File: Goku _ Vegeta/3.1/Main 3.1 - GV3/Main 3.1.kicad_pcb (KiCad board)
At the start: 2 copper layers, 206 x 197.4 mm, 64 parts, among them J1 Battery Buzzer, J10 Motor 4, J11 LEFT HEADERS, J12 RIGHT HEADERS, J13 MID HEADERS, J14 UART, J15 I2C, J16 4S Battery, J17 Power Switch, J18 Batt Bal, J19 5V PI, J2 5V LINE, J20 ESC PWR, J23 ESC PWM, J3 BACKUP 3V3, J4 I2C, J5 SPI, J6 Solenoid, J7 Motor 1, J8 Motor 2, J9 Motor 3, Q1 BSC040N10NS5, Q2 Q_Photo_NPN, U13 Adafruit_BNO055_STEMMA_QT, U4 TB67H420FTG Dual/Single Motor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, U5 TB67H420FTG Dual/Single Motor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, U6 TB67H420FTG Dual/Single Motor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, U7 TB67H420FTG Dual/Single Motor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, U8 DEV-16771, U9 Arduino Compatible DC-DC Boos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

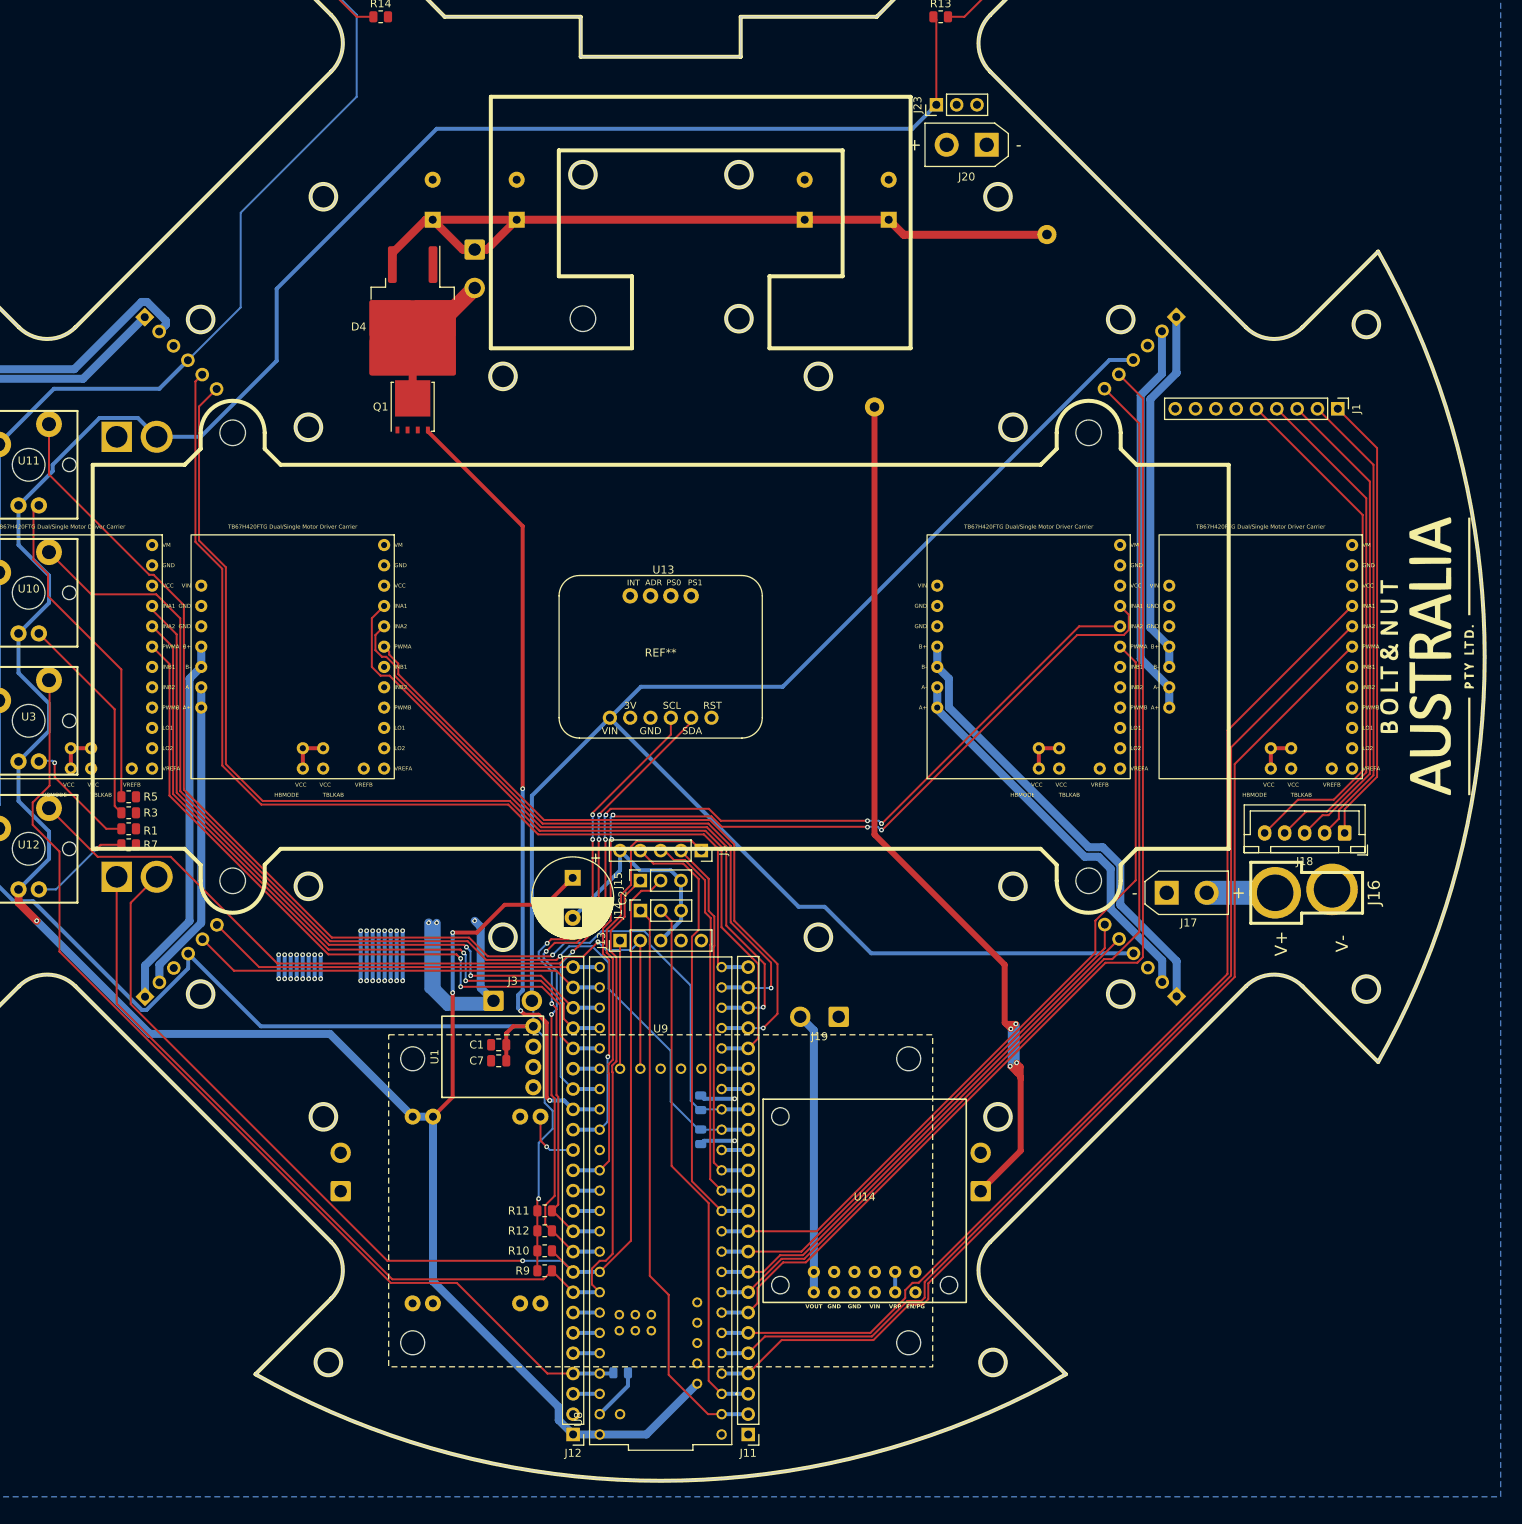
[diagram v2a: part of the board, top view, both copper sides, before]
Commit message: Main and Line 3.1 done w/ silkscreen
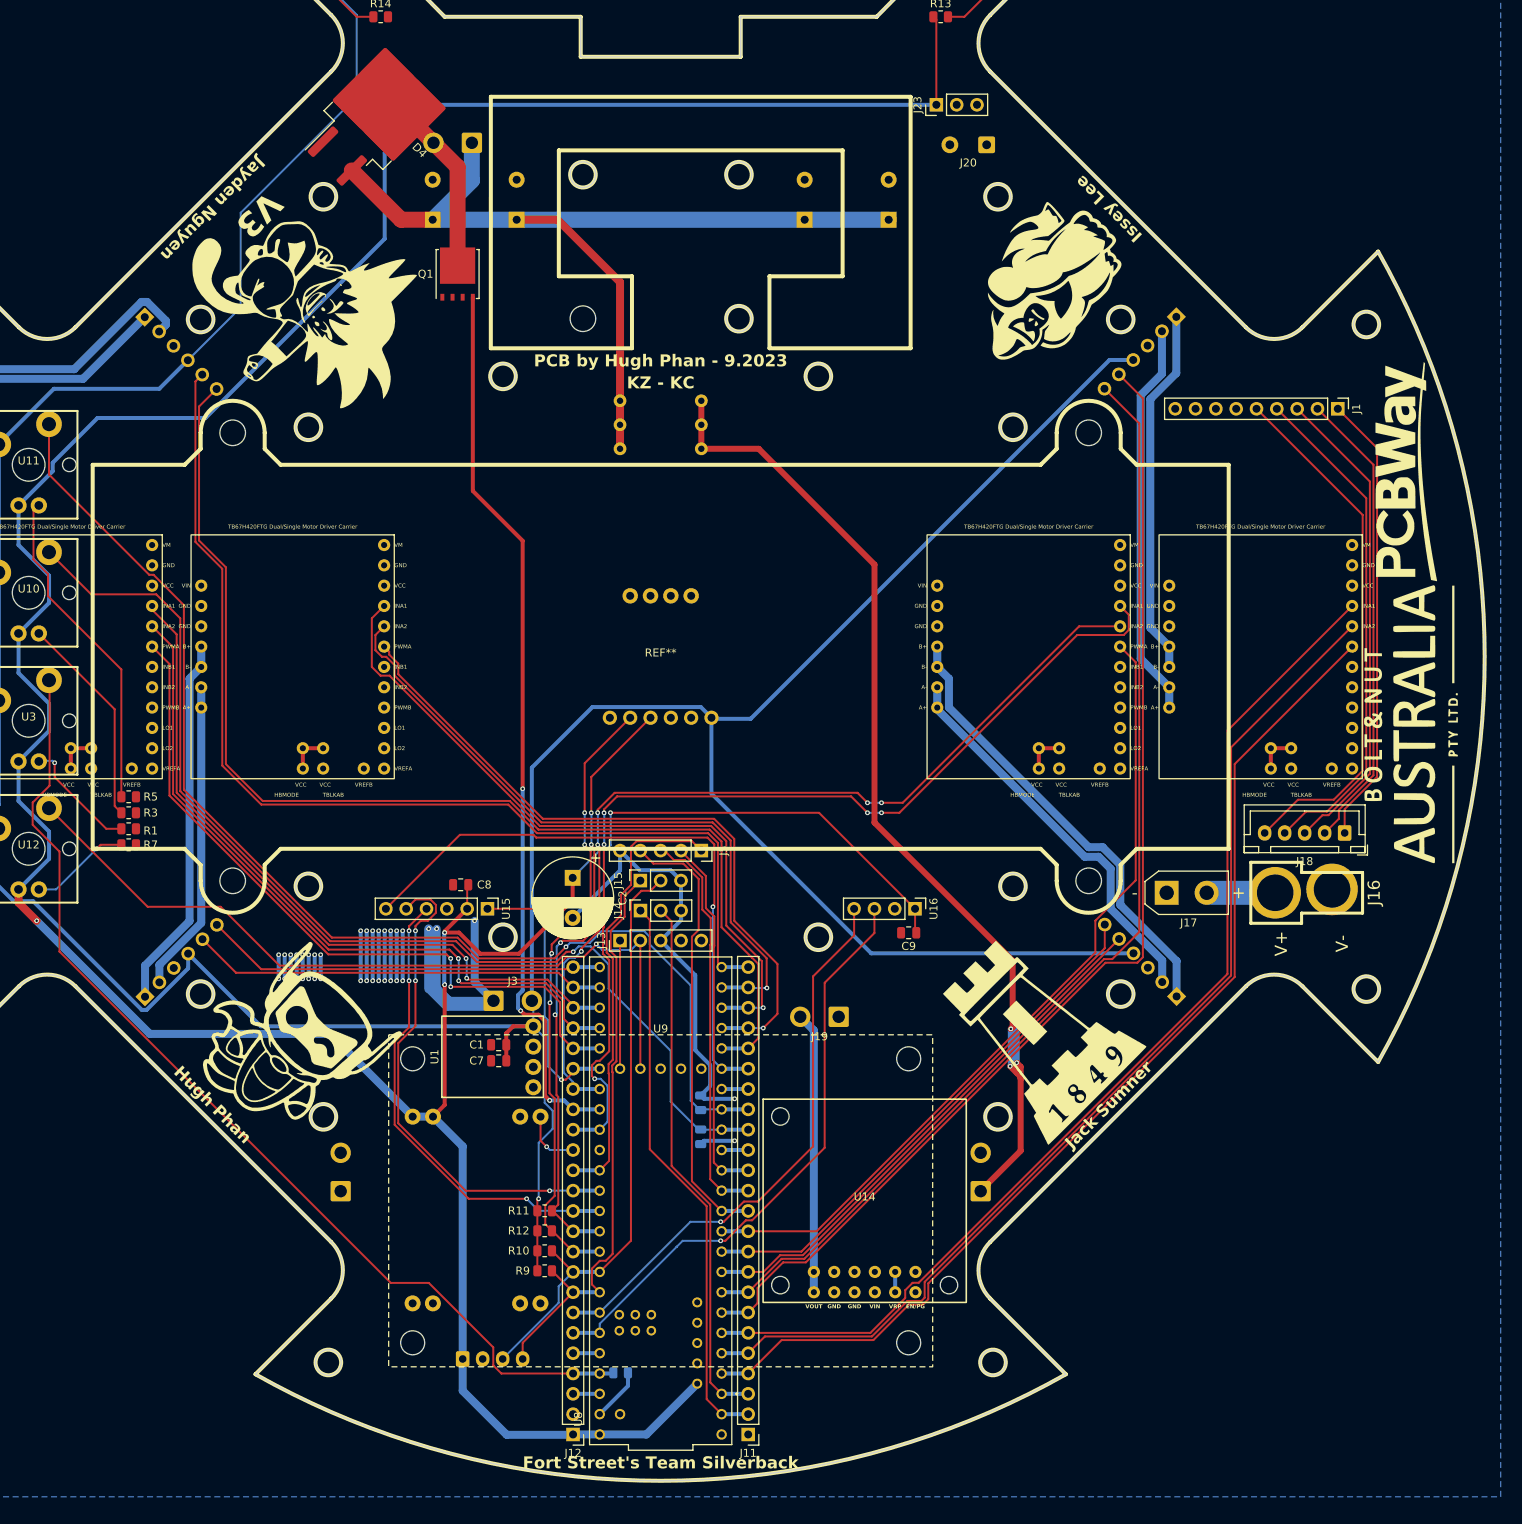
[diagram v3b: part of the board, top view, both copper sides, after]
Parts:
- removed the G*** at (245.5, 150.0)
- removed J2: 5V LINE, Connector_AMASS:AMASS_XT30U-F_1x02_P5.0mm_Vertical
- removed J4: I2C, Connector_AMASS:AMASS_XT30U-F_1x02_P5.0mm_Vertical
- added C8: 10uF, Capacitor_SMD:C_0805_2012Metric, F.Cu at (125.0, 178.5)
- added C9: 10uF, Capacitor_SMD:C_0805_2012Metric, F.Cu at (181.0, 184.5)
- added G***: LOGO, LOGO, F.Cu at (196.6, 196.4)
- added G***: LOGO, LOGO, F.Cu at (106.5, 106.0)
- added G***: LOGO, LOGO, F.Cu at (243.2, 127.0)
- added G***: LOGO, LOGO, F.Cu at (197.7, 103.3)
- added G***: LOGO, LOGO, F.Cu at (103.8, 198.0)
- added G***: LOGO, LOGO, F.Cu at (243.5, 158.5)
- added J21: Line, Connector_JST:JST_XH_B4B-XH-A_1x04_P2.50mm_Vertical, B.Cu at (125.2, 237.8)
- added R16: 15R, Resistor_THT:R_Axial_DIN0207_L6.3mm_D2.5mm_P10.16mm_Horizontal, B.Cu at (144.9, 118.0)
- added R8: 15R, Resistor_THT:R_Axial_DIN0207_L6.3mm_D2.5mm_P10.16mm_Horizontal, B.Cu at (144.9, 124.0)
- added U15: Bluetooth_Module_(HC-05), Connector_PinHeader_2.54mm:PinHeader_1x06_P2.54mm_Vertical, F.Cu at (128.3, 181.5)
- added U16: Bluetooth_Module_(HC-06), Connector_PinHeader_2.54mm:PinHeader_1x04_P2.54mm_Vertical, F.Cu at (181.8, 181.5)
- J20: footprint Connector_AMASS:AMASS_XT30UPB-F_1x02_P5.0mm_Vertical -> Connector_Wire:SolderWire-0.5sqmm_1x02_P4.6mm_D0.9mm_OD2.1mm
- R15: value 4R7 -> 15R; footprint Resistor_THT:R_Axial_Power_L25.0mm_W9.0mm_P30.48mm -> Resistor_THT:R_Axial_DIN0207_L6.3mm_D2.5mm_P10.16mm_Horizontal
- U13: moved to B.Cu
- moved R15 58.4 mm to (144.9, 121.0), turned to 0 degrees
- moved D4 26.9 mm to (115.0, 82.0), turned to 45 degrees
- moved Q1 17.5 mm to (124.6, 102.2)
- moved J6 13.4 mm to (126.4, 85.8), turned to 180 degrees
- turned U13 to 180 degrees
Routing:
- net /19: track 147.5 -> 72.7 mm
- net /27: track 3.32 -> 77.3 mm, vias 0 -> 1
- net +5V: track 383.3 -> 455.8 mm, vias 3 -> 4
- net /18: track 146.2 -> 74.3 mm, vias 1 -> 0
- net /21: track 3.33 -> 74.2 mm, vias 0 -> 1
- net /20: track 3.33 -> 70.4 mm, vias 0 -> 1
- net /14: track 3.33 -> 62.9 mm, vias 0 -> 3
- net /15: track 3.33 -> 58.8 mm, vias 0 -> 3
- net /38: track 3.33 -> 34.6 mm, vias 0 -> 2
- net GND: track 170.1 -> 191.0 mm
- net Net-(D4-A): track 99.3 -> 118.3 mm
- net /40: track 98.3 -> 112.6 mm
- net Net-(U9-OUT+): track 119.6 -> 132.3 mm
- net Net-(D4-K): track 17.9 -> 24.1 mm
- net +3V3: track 476.4 -> 472.5 mm
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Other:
- board text added: "Fort Street's Team Silverback"
- board text added: "Hugh Phan"
- board text added: "Issey Lee"
- board text added: "Jack Sumner"
- board text added: "Jayden Nguyen"
- board text added: "KZ - KC"
- board text added: "PCB by Hugh Phan - 9.2023"
- board text added: "V3"

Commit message: main 3.1 edit actualy done now i think...
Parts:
- R15, R16, R8: moved to F.Cu
- U1: moved to B.Cu
- moved C9 60.3 mm to (123.0, 201.0), turned to 0 degrees
- moved C8 52.9 mm to (174.1, 198.2)
- moved U15 51.1 mm to (177.6, 195.2)
- moved U16 51.1 mm to (132.6, 195.2)
- moved J3 49.6 mm to (130.4, 242.6)
- moved D4 37.5 mm to (120.2, 119.1), turned to -90 degrees
- moved Q1 20.2 mm to (128.8, 121.9)
- moved J19 14.0 mm to (185.9, 198.0), turned to -90 degrees
- moved J20 6.05 mm to (184.7, 86.0), turned to 0 degrees
- moved R16 6.00 mm to (144.9, 124.0)
- moved R8 6.00 mm to (144.9, 118.0)
- moved J23 5.08 mm to (189.5, 81.0), turned to -90 degrees
- moved C1 3.20 mm to (132.7, 199.8), turned to 90 degrees
- moved U1 2.55 mm to (131.3, 198.9), turned to 180 degrees
- moved G*** 1.65 mm to (106.2, 104.4)
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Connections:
- J23 pad 1: +5V -> /22
- U10 pad A: +5V -> +3V3
- U11 pad A: +5V -> +3V3
- U12 pad A: +5V -> +3V3
- U3 pad A: +5V -> +3V3
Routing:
- net /22: track 3.33 -> 201.9 mm, vias 0 -> 2
- net +5V: track 455.8 -> 318.4 mm, vias 4 -> 8
- net /27: track 77.3 -> 11.2 mm, vias 1 -> 0
- net /38: track 34.6 -> 90.7 mm, vias 2 -> 4
- net GND: track 191.0 -> 142.7 mm, vias 38 -> 35
- net +3V3: track 472.5 -> 518.0 mm, vias 1 -> 0
- net Net-(D4-K): track 24.1 -> 48.9 mm
- net /40: track 112.6 -> 89.2 mm
- net /21: track 74.2 -> 51.1 mm
- net /20: track 70.4 -> 49.3 mm
- net /14: track 62.9 -> 44.1 mm, vias 3 -> 1
- net /15: track 58.8 -> 48.0 mm, vias 3 -> 1
- net Net-(D4-A): track 118.3 -> 123.4 mm
- net /29: track 86.5 -> 83.8 mm, vias 1 -> 0
- net /18: track 74.3 -> 76.4 mm
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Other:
- outline, holes or cut-outs redrawn
